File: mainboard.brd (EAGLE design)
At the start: 93.7 x 48.2 mm, 42 parts, among them IC1 DS1307, IC2 LM2596S, J1 AVR_SPI_PRG_6PTH, Q1 32.768 kHz, U1 ATMEGA328P, U2 3.3V, U3 5V, U4 MMA7660FCR1

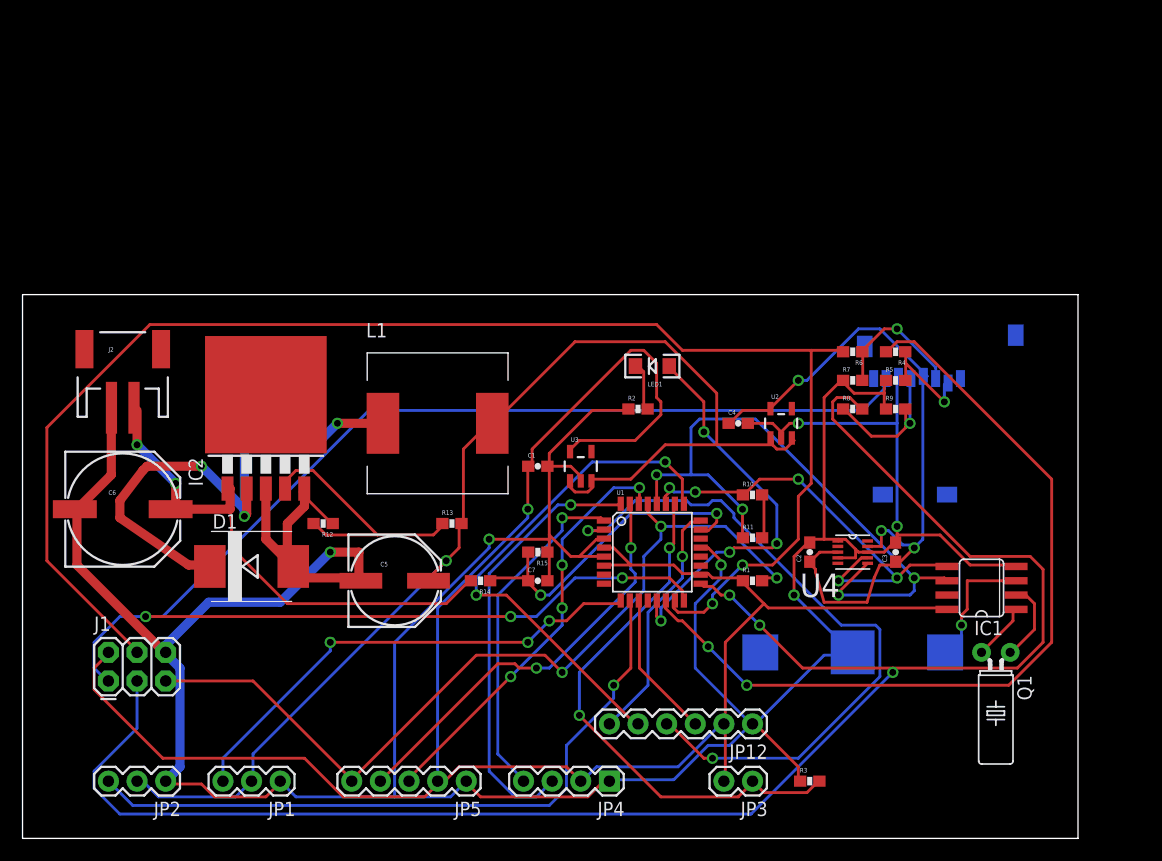
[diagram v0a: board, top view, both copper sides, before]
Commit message: Finished v1 of board design
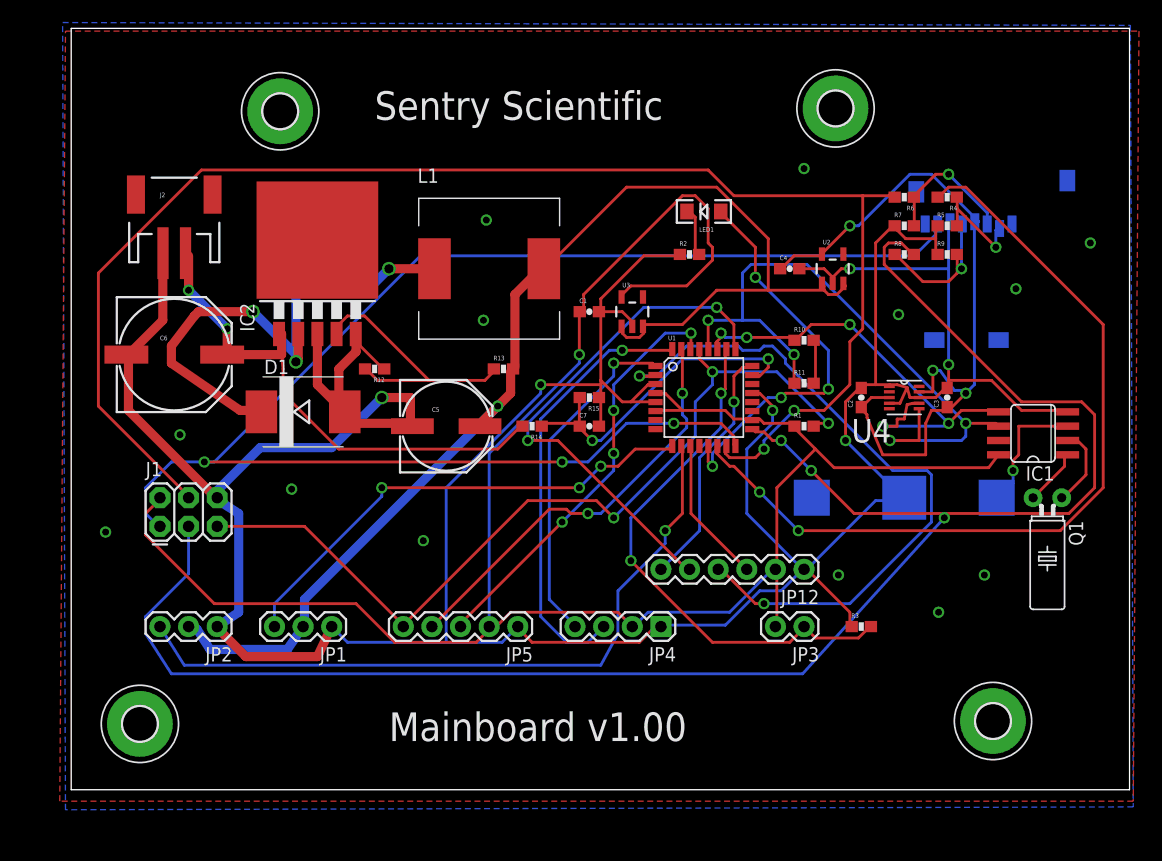
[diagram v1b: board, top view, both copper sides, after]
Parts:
- added H1, H2, H3, H4: MOUNT-PAD-ROUND3.0, holes:3,0-PAD
- moved JP3 14.5 mm to (66.8, 16.3)
- moved R1 14.5 mm to (66.8, 34.0)
- moved C2 14.5 mm to (71.9, 36.6)
- moved C5 14.5 mm to (35.1, 34.0)
- moved C6 14.5 mm to (10.9, 40.4)
- moved C7 14.5 mm to (47.8, 34.0)
- moved IC2 14.5 mm to (23.6, 48.0)
- moved J1 14.5 mm to (9.65, 25.1)
- moved J2 14.5 mm to (10.9, 53.1)
- moved JP1 14.5 mm to (24.9, 16.3)
- moved JP12 14.5 mm to (66.8, 21.3)
- moved JP2 14.5 mm to (14.7, 16.3)
- moved JP5 14.5 mm to (41.4, 16.3)
- moved L1 14.5 mm to (38.9, 48.0)
- moved R10 14.5 mm to (66.8, 41.7)
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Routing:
- net GND: track 335.9 -> 338.8 mm, vias 6 -> 19
- net +3.3V: track 62.9 -> 65.2 mm
- net SDA: track 40.0 -> 42.1 mm
- net RIGHTSERVO: track 61.2 -> 63.2 mm
- net SCK: track 158.3 -> 160.2 mm
- net SCL: track 59.1 -> 60.6 mm
- net +5V: track 182.8 -> 183.9 mm
- net +6V: track 108.3 -> 109.2 mm
- net MISO: track 134.9 -> 134.3 mm
- added copper zone on layer 1, net GND
- added copper zone on layer 16, net GND
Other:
- board size 93.7 x 48.2 mm -> 93.9 x 67.6 mm
- board text added: "Mainboard v1.00"
- board text added: "Sentry Scientific"

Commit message: Updates
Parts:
- removed H1, H2, H3, H4: MOUNT-PAD-ROUND3.0, holes:3,0-PAD
- removed JP12: Extra, SparkFun-Connectors:1X06
- added JP6: Extra, SparkFun-Connectors:1X04
- added JP7: MAIN_SW, SparkFun-Connectors:1X02
- added LED2: (no value), SparkFun-LED:LED-1206
- added R16: 100, SparkFun-Resistors:0603-RES
- added R17: 10k, SparkFun-Resistors:0603-RES
- moved C2 9.72 mm to (68.6, 27.4)
- moved C3 9.72 mm to (76.2, 27.4), turned to 270 degrees
- moved U4 9.72 mm to (72.4, 27.4)
- moved R2 9.25 mm to (65.3, 52.6), turned to 180 degrees
- moved R3 6.65 mm to (72.6, 22.9)
- moved JP3 6.35 mm to (72.9, 18.0)
- moved C1 4.79 mm to (51.8, 46.7), turned to 270 degrees
- moved U3 4.49 mm to (54.9, 47.2)
- moved U2 4.35 mm to (65.0, 47.5)
- moved R11 3.84 mm to (70.6, 37.3)
- moved R1 3.82 mm to (70.6, 33.8)
- moved R10 3.82 mm to (70.6, 41.4)
- moved R14 3.75 mm to (46.0, 35.8)
- moved C4 3.70 mm to (62.0, 47.0), turned to 270 degrees
- moved R15 3.10 mm to (46.0, 39.1)
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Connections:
- removed net D4: JP12.4, U1.2
- removed net D7: JP12.3, U1.11
- new net 6V_ON: IC2.5, U1.2
- new net MAIN_SW: JP7.2, R17.1, U1.11
- new net N$12: LED2.C, R16.2
- new net N$13: LED2.A, U1.12
- net +5V: now also JP6.2, R17.2; no longer JP12.2
- net +6V: no longer U2.1, U2.3, U3.1, U3.3
- net A1: now also JP6.4; no longer JP12.6
- net A2: now also JP6.3; no longer JP12.5
- net BAT+: now also U2.1, U2.3, U3.1, U3.3
- net GND: now also JP6.1, JP7.1, R16.1; no longer IC2.5, JP12.1
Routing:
- net D4: track 61.1 -> 0.00 mm, vias 2 -> 0
- net BAT+: track 45.5 -> 103.9 mm
- net +6V: track 109.2 -> 51.9 mm, vias 1 -> 0
- net SCK: track 160.2 -> 107.8 mm
- net MAIN_SW: track 0.00 -> 40.1 mm, vias 0 -> 1
- net N$13: track 0.00 -> 32.8 mm, vias 0 -> 2
- net 6V_ON: track 0.00 -> 29.7 mm, vias 0 -> 2
- net SD_CS: track 73.9 -> 51.3 mm
- net N$10: track 47.6 -> 26.1 mm, vias 3 -> 0
- net MOSI: track 130.9 -> 151.2 mm
- net GND: track 338.8 -> 354.2 mm, vias 19 -> 2
- net +5V: track 183.9 -> 170.3 mm, vias 1 -> 4
- net RESET: track 76.8 -> 90.3 mm, vias 3 -> 4
- net D7: track 13.0 -> 0.00 mm
- net SDA: track 42.1 -> 55.1 mm, vias 5 -> 0
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- removed copper zone on layer 1, net GND
- removed copper zone on layer 16, net GND
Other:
- board size 93.9 x 67.6 mm -> 93.9 x 49.3 mm
- board text added: "+5"
- board text added: "2013 Sentry Scientific"
- board text added: "A"
- board text added: "B"
- board text added: "G"
- board text added: "I"
- board text added: "O"
- board text added: "R"
- board text added: "RES"
- board text added: "T"
- board text removed: "Sentry Scientific"

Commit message: Bring it up to date
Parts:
- R15: value 780k -> 470k
- moved C4 11.1 mm to (60.2, 36.1)
- moved C6 11.1 mm to (9.14, 29.5)
- moved LED1 11.1 mm to (57.7, 41.7)
- moved LED2 11.1 mm to (57.7, 45.0)
- moved R16 11.1 mm to (63.5, 45.0)
- moved R2 11.1 mm to (63.5, 41.7)
- moved IC1 11.1 mm to (86.6, 22.1)
- moved R4 11.1 mm to (77.7, 43.4)
- moved R5 11.1 mm to (77.7, 40.9)
- moved R6 11.1 mm to (73.9, 43.4)
- moved R7 11.1 mm to (73.9, 40.9)
- moved R8 11.1 mm to (73.9, 38.4)
- moved R9 11.1 mm to (77.7, 38.4)
- moved C5 11.1 mm to (33.3, 23.1)
- moved J1 11.1 mm to (6.10, 14.2)
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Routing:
- net GND: vias 2 -> 7
- added copper zone on layer 1, net GND
- added copper zone on layer 16, net GND
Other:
- board text added: "^__^ (oo)\_______ (__)\ )\/\ ||----w | || ||"

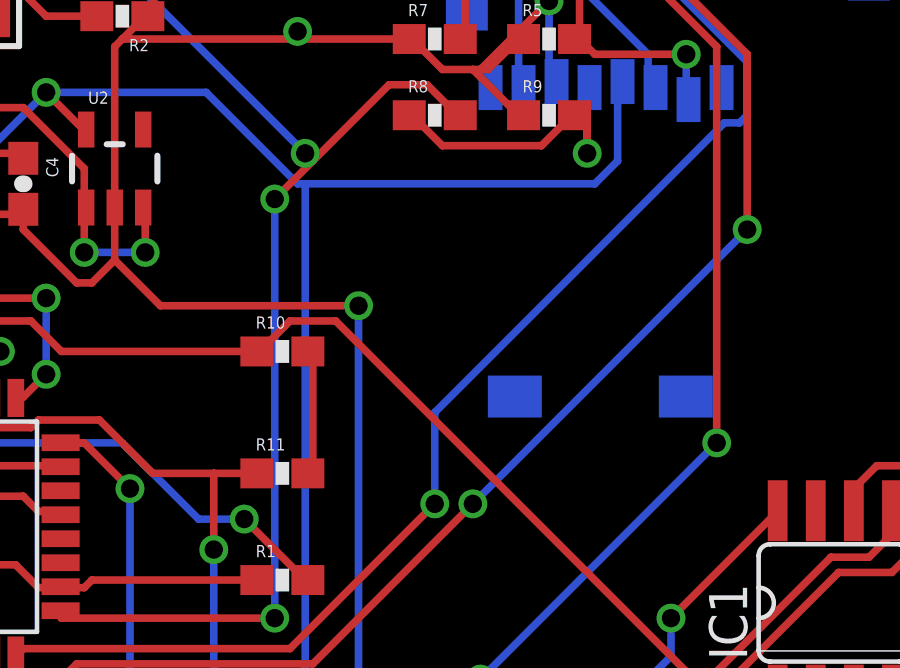
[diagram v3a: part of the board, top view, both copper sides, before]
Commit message: Changed instances of 3.3V net to correct +3.3V net. Rerouted affected sections.
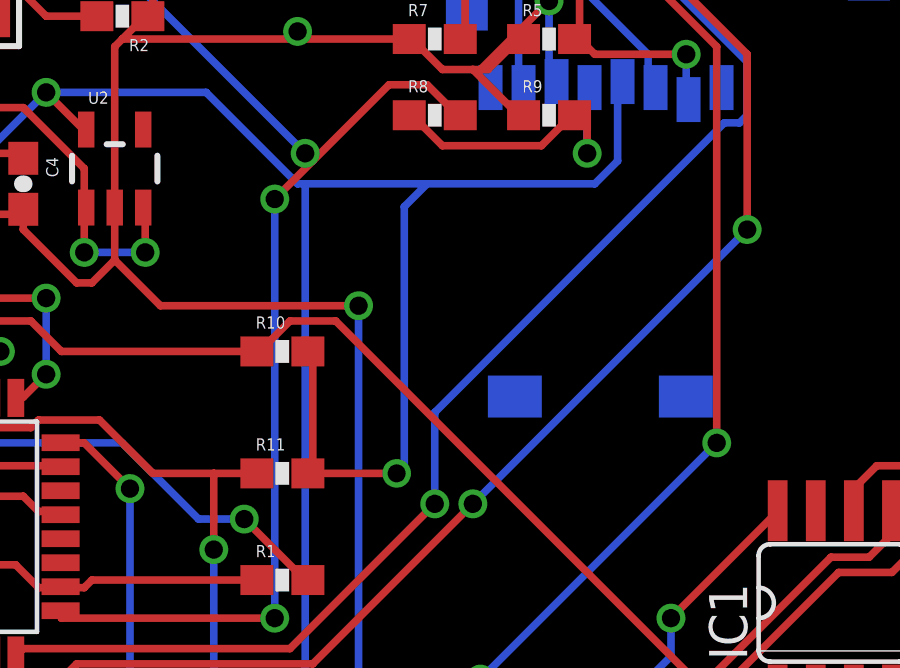
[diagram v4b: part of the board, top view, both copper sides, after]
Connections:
- removed net 3.3V: R10.2, R11.2
- net +3.3V: now also R10.2, R11.2
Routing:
- net +3.3V: track 61.6 -> 78.7 mm, vias 3 -> 4
- net 3.3V: track 4.40 -> 0.00 mm
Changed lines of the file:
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@@
 <wire x1="79.248" y1="36.068" x2="80.01" y2="36.83" width="0.254" layer="16"/>
 <wire x1="69.342" y1="36.068" x2="69.596" y2="36.068" width="0.254" layer="16"/>
-<wire x1="69.596" y1="36.068" x2="79.248" y2="36.068" width="0.254" layer="16"/>
+<wire x1="69.596" y1="36.068" x2="73.66" y2="36.068" width="0.254" layer="16"/>
+<wire x1="73.66" y1="36.068" x2="79.248" y2="36.068" width="0.254" layer="16"/>
 <wire x1="66.294" y1="39.116" x2="69.342" y2="36.068" width="0.254" layer="16"/>
 <wire x1="60.96" y1="39.116" x2="66.294" y2="39.116" width="0.254" layer="16"/>
@@
 <via x="60.96" y="39.116" extent="1-16" drill="0.6096"/>
 <via x="69.596" y="18.542" extent="1-16" drill="0.6096"/>
-</signal>
-<signal name="3.3V">
 <contactref element="R10" pad="2"/>
 <contactref element="R11" pad="2"/>
 <wire x1="69.85" y1="30.48" x2="69.85" y2="26.416" width="0.254" layer="1"/>
 <wire x1="69.85" y1="26.416" x2="69.684" y2="26.416" width="0.254" layer="1"/>
-<wire x1="69.85" y1="30.48" x2="69.684" y2="30.48" width="0.254" layer="1"/>
+<wire x1="73.66" y1="36.068" x2="72.898" y2="35.306" width="0.254" layer="16"/>
+<wire x1="72.898" y1="35.306" x2="72.898" y2="26.67" width="0.254" layer="16"/>
+<wire x1="72.898" y1="26.67" x2="72.644" y2="26.416" width="0.254" layer="16"/>
+<via x="72.644" y="26.416" extent="1-16" drill="0.6"/>
+<wire x1="72.644" y1="26.416" x2="69.85" y2="26.416" width="0.254" layer="1"/>
+<wire x1="69.85" y1="30.48" x2="69.684" y2="30.48" width="0" layer="19" extent="1-1"/>
 </signal>
 <signal name="N$7">

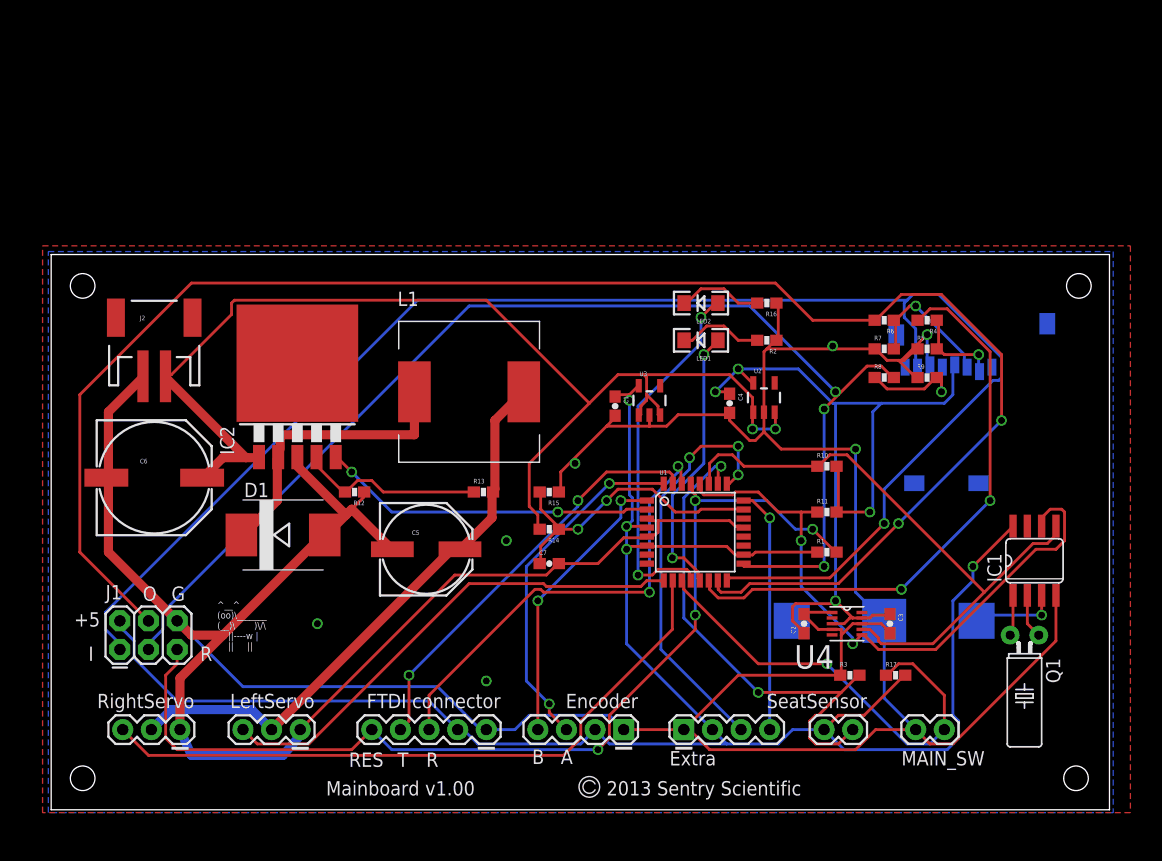
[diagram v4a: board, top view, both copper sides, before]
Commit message: added lbr for MMA8653. changed accelerometer to MMA8653.
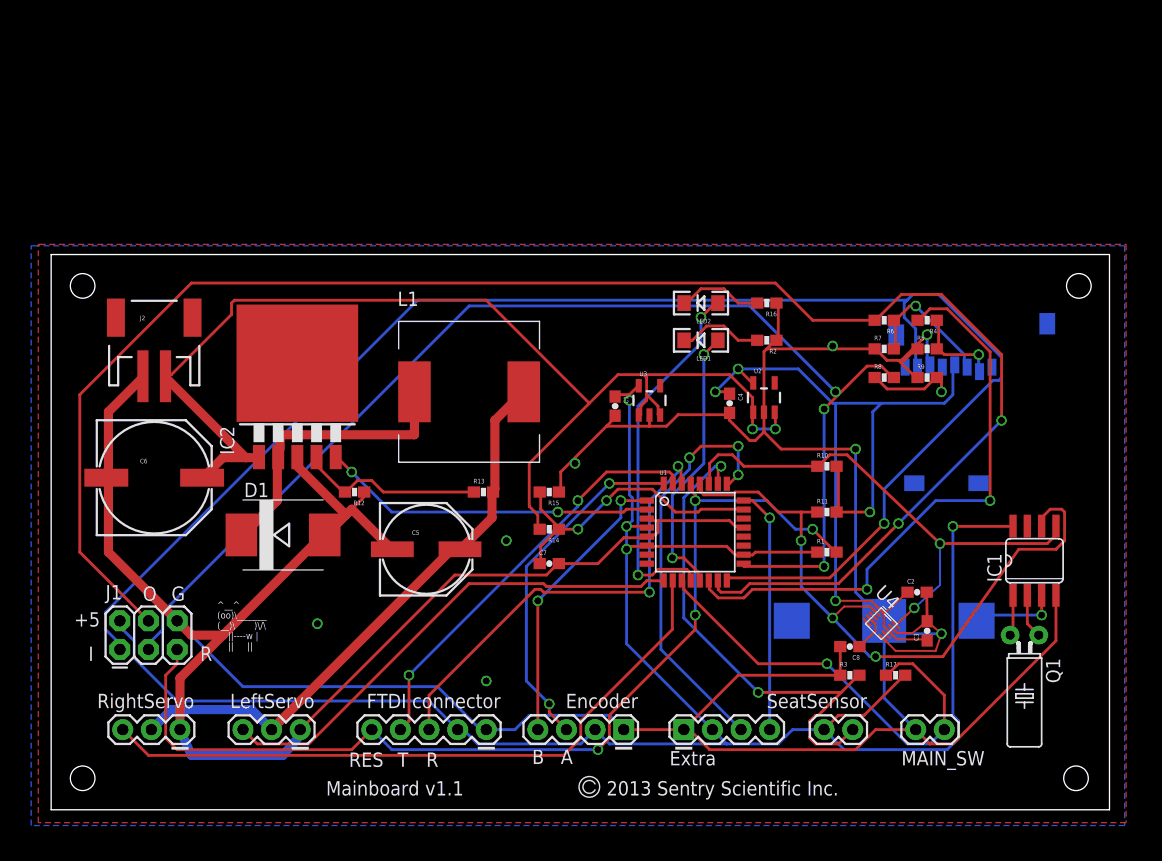
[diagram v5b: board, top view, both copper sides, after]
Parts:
- added C8: 0.1uF, SparkFun-Capacitors:0603-CAP
- C2: value 0.1uF -> 1uF
- U4: value MMA7660FCR1 -> MMA8653FC; device Freescale_By_element14_Batch_1:DFN300X300X100-10N -> logic-supply:DFN10-2X2
- moved C2 10.4 mm to (76.8, 19.3), turned to 0 degrees
- moved C3 3.36 mm to (77.7, 15.9), turned to 90 degrees
- moved U4 3.05 mm to (73.7, 16.5), turned to 315 degrees
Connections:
- new net N$16: C8.1, U4.4
- net +3.3V: now also U4.1, U4.8; no longer U4.3, U4.9
- net GND: now also C8.2, U4.6, U4.7, U4.9; no longer U4.1, U4.4, U4.8
- net SCL: now also U4.2; no longer U4.6
- net SDA: now also U4.10; no longer U4.7
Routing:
- net SDA: track 55.1 -> 47.0 mm, vias 0 -> 2
- net GND: track 354.2 -> 362.2 mm, vias 7 -> 8
- net SCL: track 55.0 -> 60.1 mm, vias 2 -> 3
- net N$16: track 0.00 -> 3.28 mm
- net +5V: track 170.3 -> 173.4 mm
- net +3.3V: track 78.7 -> 77.3 mm
- net SD_CS: track 51.3 -> 52.3 mm
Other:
- board text added: "2013 Sentry Scientific Inc."
- board text added: "Mainboard v1.1"
- board text removed: "2013 Sentry Scientific"
- board text removed: "Mainboard v1.00"
